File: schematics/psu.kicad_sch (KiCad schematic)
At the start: 32 parts, among them Q1 Si9933CDY, Q2 BSS138, U10 LTC4002ES8, U11 MAX604, U12 MAX604, U9 BQ29200

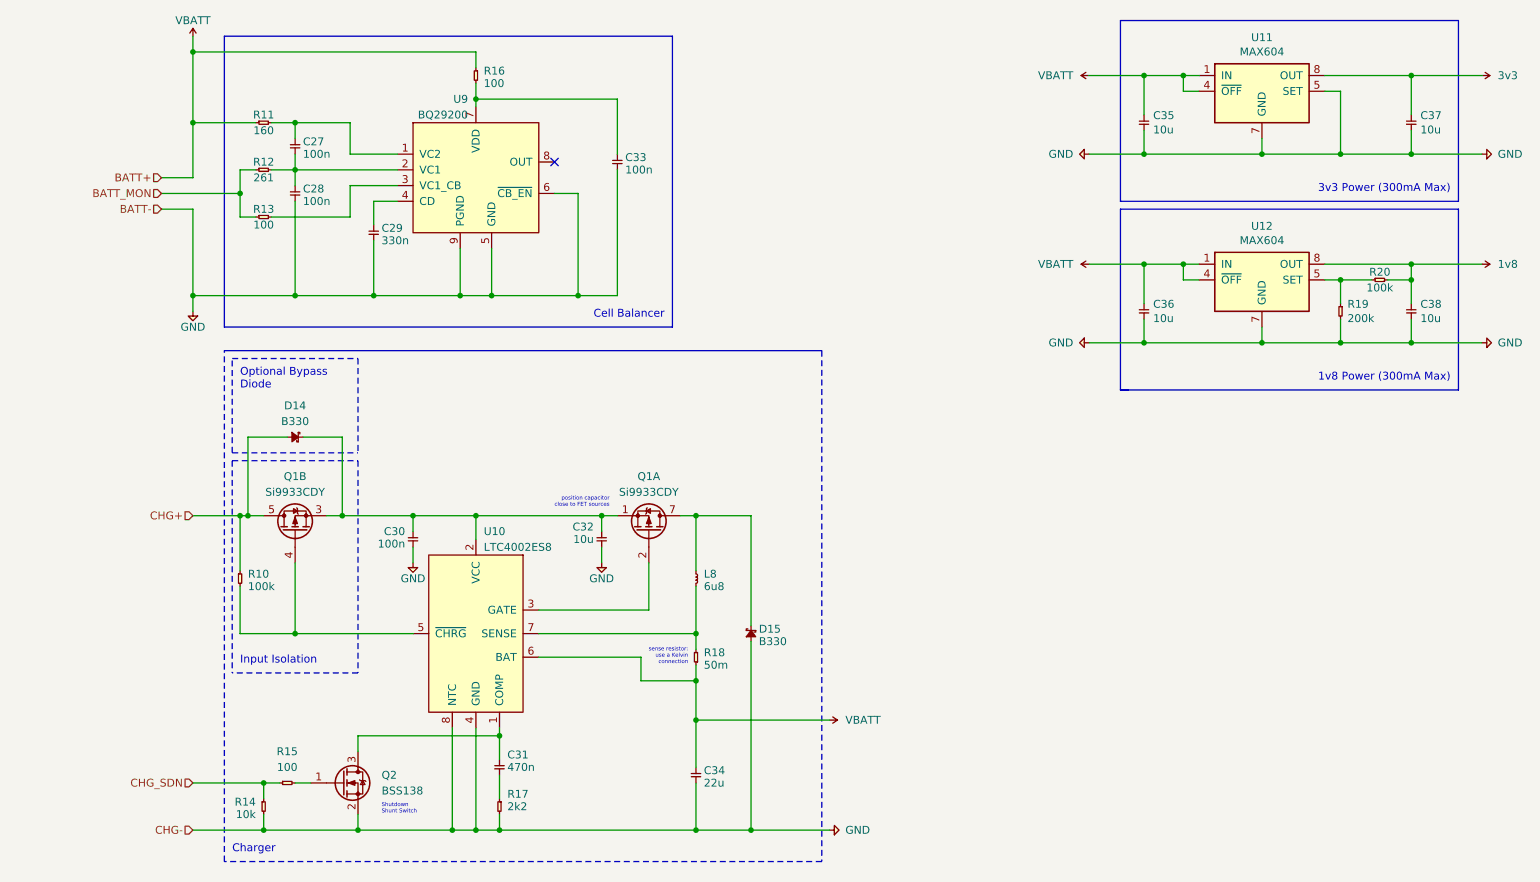
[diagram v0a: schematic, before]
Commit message: Add oscillators and clean up schematics
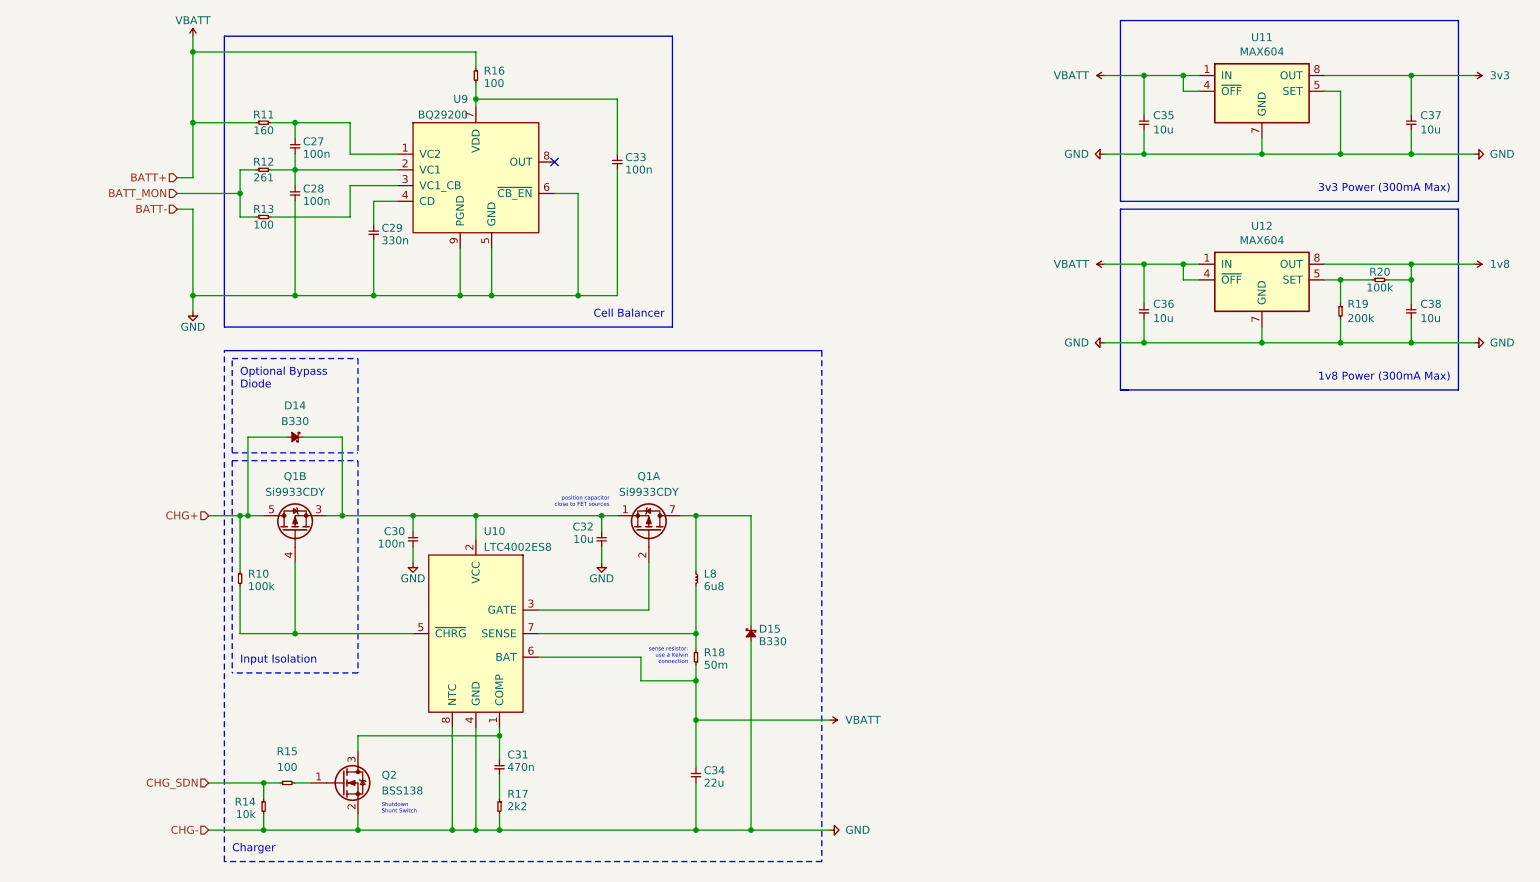
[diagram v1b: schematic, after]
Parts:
- C27, C28, C29, C30, C31, C32, C33, C34: footprint Battery:C_0805_2012Metric_Pad1.18x1.45mm_HandSolder -> Strix:C_0402
- D14, D15: footprint Battery:D_SMB_Handsoldering -> Strix:B330
- L8: footprint Battery:L_Wuerth_HCI-7050 -> Strix:L_Wuerth_HCI-7050
- R10, R11, R12, R13, R14, R15, R16, R17, R18: footprint Battery:R_0805_2012Metric_Pad1.20x1.40mm_HandSolder -> Strix:R_0402

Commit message: Fix broken symbol and footprint references
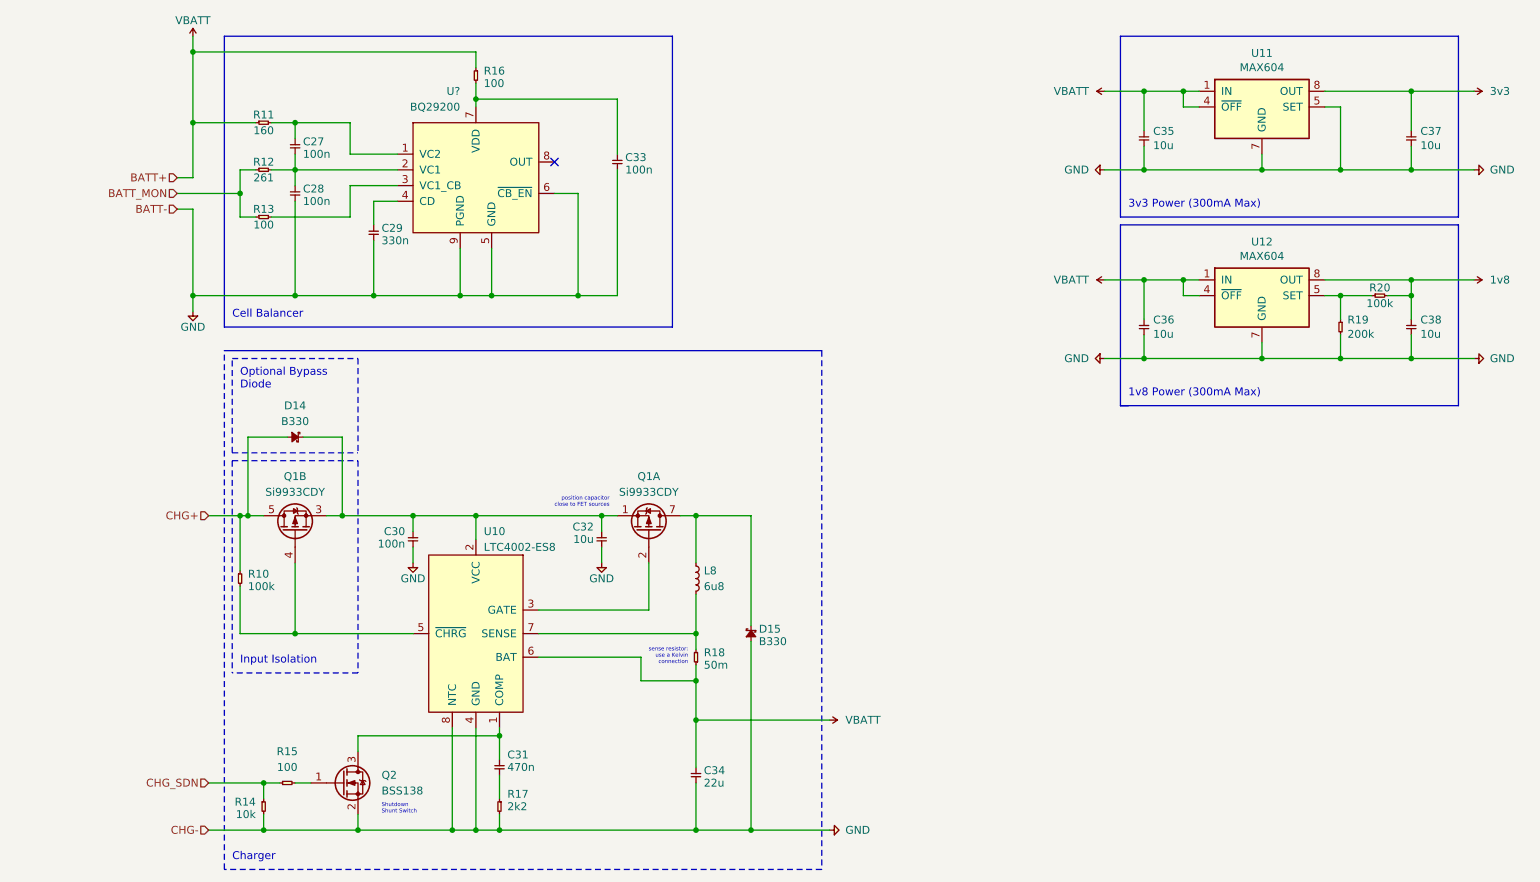
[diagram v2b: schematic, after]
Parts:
- removed U9: BQ29200, Battery:BQ2920X, symbol Battery:BQ2920X
- added U?: BQ29200, Strix:BQ29200, symbol Strix:BQ29200
- C27, C28, C29, C30, C31, C32, C33, C34: symbol Battery:C -> Strix:C
- D14, D15: symbol Battery:B330 -> Strix:B330
- L8: symbol Battery:L -> Strix:L_Large
- Q1: footprint Battery:SOIC-8_3.9x4.9mm_P1.27mm -> Strix:Si9933CDY; symbol Battery:Si9933CDY -> Strix:Si9933CDY
- Q2: footprint Package_TO_SOT_SMD:SOT-23 -> Strix:BSS138
- R10, R11, R12, R13, R14, R15, R16, R17, R18: symbol Battery:R -> Strix:R
- U10: value LTC4002ES8 -> LTC4002-ES8; footprint Battery:SO-8_3.9x4.9mm_P1.27mm -> Strix:LTC4002-ES8; symbol Battery:LTC4002ES8 -> Strix:LTC4002-ES8
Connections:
- net GND: now also U?.5 (GND), U?.6 (~{CB_EN}), U?.9 (PGND)
- net at C33.1, R16.2: now also U?.7 (VDD)
- net at C27.2, C28.1, R12.2: now also U?.2 (VC1)
- net at C27.1, R11.2: now also U?.1 (VC2)
- net at C29.1: now also U?.4 (CD)
- net at R13.2: now also U?.3 (VC1_CB)
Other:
- moved on the sheet: C35, C36, C37, C38, R19, R20, U11, U12

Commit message: Add missing IC footprints
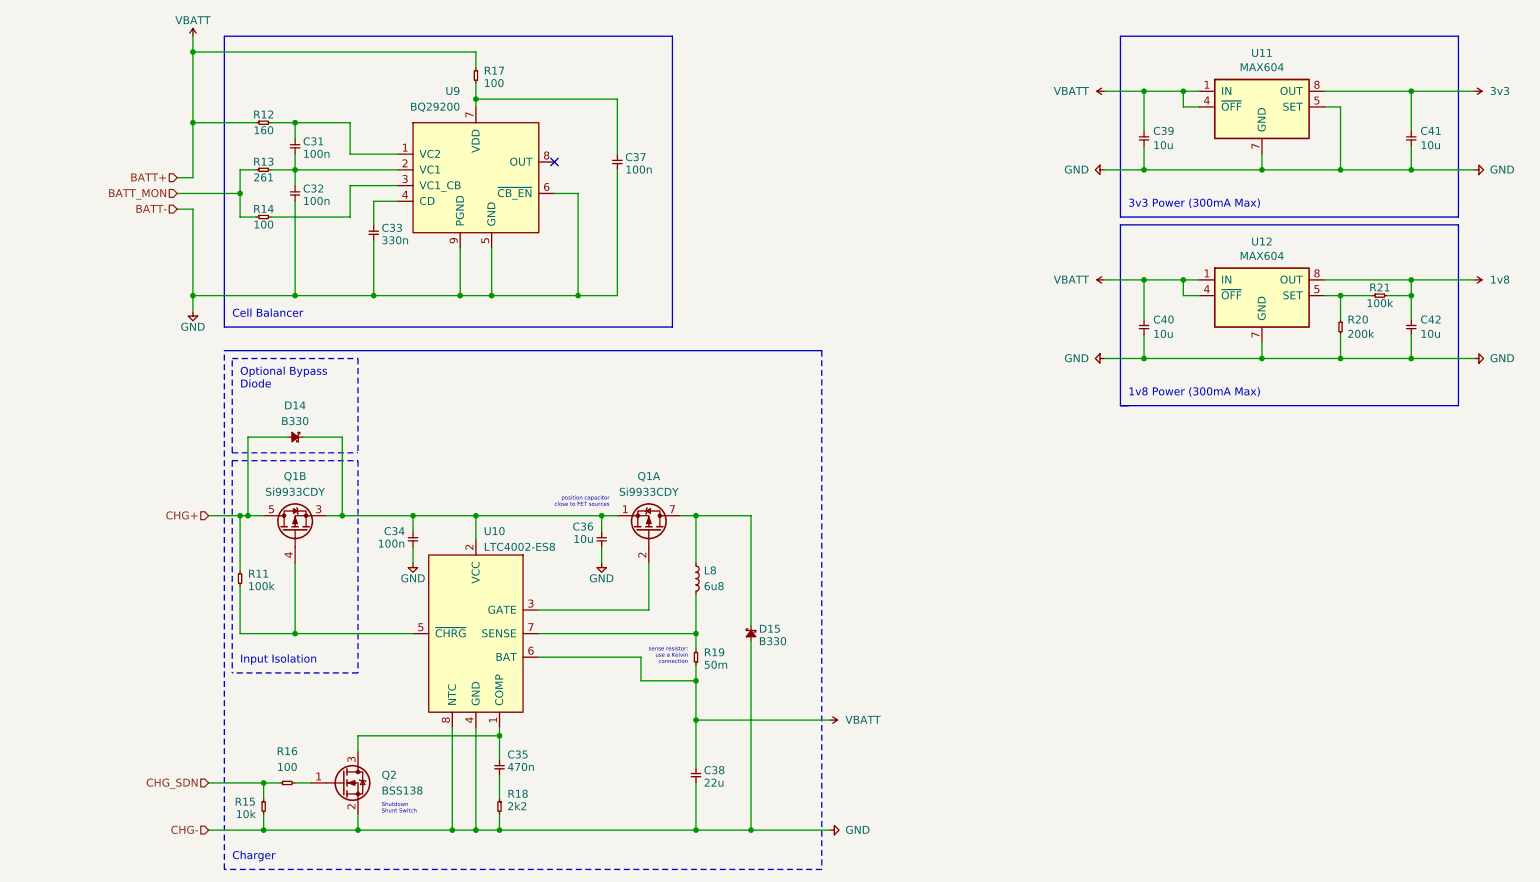
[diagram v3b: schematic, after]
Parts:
- gave numbers to parts that had none: 1
- renumbered C27 to C31, C28 to C32, C29 to C33, C30 to C34, C31 to C35, C32 to C36, C33 to C37, C34 to C38, C35 to C39, C36 to C40, C37 to C41, C38 to C42, R10 to R11, R11 to R12, R12 to R13, R13 to R14, R14 to R15, R15 to R16, R16 to R17, R17 to R18, R18 to R19, R19 to R20, R20 to R21

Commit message: Preliminary board layout
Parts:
- renumbered D14 to D15, D15 to D16
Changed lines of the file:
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@@
   (symbol (lib_id "Strix:GND") (at 255.27 64.77 90) (unit 1)
     (in_bom yes) (on_board yes)
-    (property "Reference" "#PWR055" (id 0) (at 254.254 68.072 0)
+    (property "Reference" "#PWR056" (id 0) (at 254.254 68.072 0)
       (effects (font (size 1.27 1.27)) (justify left) hide)
     )
@@
   (symbol (lib_id "Strix:GND") (at 48.26 87.63 0) (mirror y) (unit 1)
     (in_bom yes) (on_board yes)
-    (property "Reference" "#PWR045" (id 0) (at 51.562 86.614 0)
+    (property "Reference" "#PWR046" (id 0) (at 51.562 86.614 0)
       (effects (font (size 1.27 1.27)) (justify left) hide)
     )
@@
   (symbol (lib_id "Strix:VBATT") (at 195.58 82.55 90) (unit 1)
     (in_bom yes) (on_board yes)
-    (property "Reference" "#PWR052" (id 0) (at 192.786 82.55 0)
+    (property "Reference" "#PWR053" (id 0) (at 192.786 82.55 0)
       (effects (font (size 1.27 1.27)) (justify left) hide)
     )
@@
   (symbol (lib_id "Strix:VBATT") (at 195.58 52.07 90) (unit 1)
     (in_bom yes) (on_board yes)
-    (property "Reference" "#PWR050" (id 0) (at 192.786 52.07 0)
+    (property "Reference" "#PWR051" (id 0) (at 192.786 52.07 0)
       (effects (font (size 1.27 1.27)) (justify left) hide)
     )
@@
   (symbol (lib_id "Strix:VBATT") (at 151.13 153.67 270) (unit 1)
     (in_bom yes) (on_board yes)
-    (property "Reference" "#PWR048" (id 0) (at 153.924 153.67 0)
+    (property "Reference" "#PWR049" (id 0) (at 153.924 153.67 0)
       (effects (font (size 1.27 1.27)) (justify left) hide)
     )
@@
   (symbol (lib_name "B330_1") (lib_id "Strix:B330") (at 66.04 107.95 0) (mirror y) (unit 1)
     (in_bom yes) (on_board yes)
-    (property "Reference" "D14" (id 0) (at 64.77 102.87 0))
+    (property "Reference" "D15" (id 0) (at 64.77 102.87 0))
     (property "Value" "B330" (id 1) (at 64.77 105.41 0))
     (property "Footprint" "Strix:B330" (id 2) (at 67.31 108.712 0)
@@
   (symbol (lib_id "Strix:GND") (at 195.58 95.25 270) (unit 1)
     (in_bom yes) (on_board yes)
-    (property "Reference" "#PWR053" (id 0) (at 196.596 91.948 0)
+    (property "Reference" "#PWR054" (id 0) (at 196.596 91.948 0)
       (effects (font (size 1.27 1.27)) (justify left) hide)
     )
@@
   (symbol (lib_id "Strix:GND") (at 114.3 128.27 0) (mirror y) (unit 1)
     (in_bom yes) (on_board yes)
-    (property "Reference" "#PWR047" (id 0) (at 117.602 127.254 0)
+    (property "Reference" "#PWR048" (id 0) (at 117.602 127.254 0)
       (effects (font (size 1.27 1.27)) (justify left) hide)
     )
@@
   (symbol (lib_id "Strix:GND") (at 195.58 64.77 270) (unit 1)
     (in_bom yes) (on_board yes)
-    (property "Reference" "#PWR051" (id 0) (at 196.596 61.468 0)
+    (property "Reference" "#PWR052" (id 0) (at 196.596 61.468 0)
       (effects (font (size 1.27 1.27)) (justify left) hide)
     )
@@
   (symbol (lib_id "Strix:GND") (at 255.27 95.25 90) (unit 1)
     (in_bom yes) (on_board yes)
-    (property "Reference" "#PWR057" (id 0) (at 254.254 98.552 0)
+    (property "Reference" "#PWR058" (id 0) (at 254.254 98.552 0)
       (effects (font (size 1.27 1.27)) (justify left) hide)
     )
@@
   (symbol (lib_id "Strix:VBATT") (at 48.26 43.18 0) (mirror y) (unit 1)
     (in_bom yes) (on_board yes)
-    (property "Reference" "#PWR044" (id 0) (at 48.26 40.386 0)
+    (property "Reference" "#PWR045" (id 0) (at 48.26 40.386 0)
       (effects (font (size 1.27 1.27)) (justify left) hide)
     )
@@
   (symbol (lib_id "Strix:1v8") (at 255.27 82.55 270) (unit 1)
     (in_bom yes) (on_board yes)
-    (property "Reference" "#PWR056" (id 0) (at 258.064 82.55 0)
+    (property "Reference" "#PWR057" (id 0) (at 258.064 82.55 0)
       (effects (font (size 1.27 1.27)) (justify left) hide)
     )
@@
   (symbol (lib_id "Strix:3v3") (at 255.27 52.07 270) (unit 1)
     (in_bom yes) (on_board yes)
-    (property "Reference" "#PWR054" (id 0) (at 258.064 52.07 0)
+    (property "Reference" "#PWR055" (id 0) (at 258.064 52.07 0)
       (effects (font (size 1.27 1.27)) (justify left) hide)
     )
@@
   (symbol (lib_id "Strix:GND") (at 151.13 171.45 90) (unit 1)
     (in_bom yes) (on_board yes)
-    (property "Reference" "#PWR049" (id 0) (at 150.114 174.752 0)
+    (property "Reference" "#PWR050" (id 0) (at 150.114 174.752 0)
       (effects (font (size 1.27 1.27)) (justify left) hide)
     )
@@
   (symbol (lib_id "Strix:B330") (at 138.43 138.43 90) (mirror x) (unit 1)
     (in_bom yes) (on_board yes)
-    (property "Reference" "D15" (id 0) (at 139.7 139.7 90)
+    (property "Reference" "D16" (id 0) (at 139.7 139.7 90)
       (effects (font (size 1.27 1.27)) (justify right bottom))
     )
@@
   (symbol (lib_id "Strix:GND") (at 83.82 128.27 0) (unit 1)
     (in_bom yes) (on_board yes)
-    (property "Reference" "#PWR046" (id 0) (at 80.518 127.254 0)
-      (effects (font (size 1.27 1.27)) (justify left) hide)
-    )
+    (property "Reference" "#PWR047" (id 0) (at 80.518 127.254 0)
+      (effects (font (size 1.27 1.27)) (justify left) hide)
+    )
